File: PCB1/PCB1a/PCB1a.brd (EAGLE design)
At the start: 125.6 x 84.2 mm, 0 parts

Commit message: ,,
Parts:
- added HUB08RG, HUB12RG, HUB75RGB, HUB75RGB.: 61231620621, Wurth_Connectors_WR-BHD:61231620621
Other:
- board text added: "HUB08 RG"
- board text added: "HUB12 RG"
- board text added: "HUB75 RGB"

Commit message: .
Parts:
- added J1: 691318400002, Wurth_Connectors_WR-TBL Pluggable Connector:691318400002
- added J2: 691317410002, Wurth_Connectors_WR-TBL Pluggable Connector:691317410002
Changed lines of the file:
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@@
 <attribute name="WORKING-VOLTAGE" value="250V(AC)" x="-60.96" y="0" locked="yes" size="1.778" layer="27" display="off"/>
+</element>
+<element name="J1" library="Wurth_Connectors_WR-TBL Pluggable Connector" library_urn="urn:adsk.eagle:library:16280984" package="691318400002" package3d_urn="urn:adsk.eagle:package:16282433/2" value=" 691318400002 " x="30.48" y="48.26" smashed="yes">
+<attribute name="DATASHEET-URL" value="https://www.we-online.com/redexpert/spec/691318400002?ae" x="30.48" y="48.26" size="1.778" layer="27" display="off"/>
+<attribute name="IR-UL" value="20A" x="30.48" y="48.26" size="1.778" layer="27" display="off"/>
+<attribute name="MOUNT" value="THT" x="30.48" y="48.26" size="1.778" layer="27" display="off"/>
+<attribute name="NAME" x="30.48" y="53.76" size="1.27" layer="25" align="bottom-center"/>
+<attribute name="PART-NUMBER" value=" 691318400002 " x="30.48" y="48.26" size="1.778" layer="27" display="off"/>
+<attribute name="PINS" value=" 2 " x="30.48" y="48.26" size="1.778" layer="27" display="off"/>
+<attribute name="PITCH" value="7.62mm" x="30.48" y="48.26" size="1.778" layer="27" display="off"/>
+<attribute name="TYPE" value="Vertical" x="30.48" y="48.26" size="1.778" layer="27" display="off"/>
+<attribute name="VALUE" x="26.98" y="42.26" size="1.27" layer="27"/>
+<attribute name="WORKING-VOLTAGE-UL" value="300V (AC)" x="30.48" y="48.26" size="1.778" layer="27" display="off"/>
+</element>
+<element name="J2" library="Wurth_Connectors_WR-TBL Pluggable Connector" library_urn="urn:adsk.eagle:library:16280984" package="691317410002" package3d_urn="urn:adsk.eagle:package:16282458/2" value=" 691317410002 " x="-73.66" y="-60.96" smashed="yes">
+<attribute name="DATASHEET-URL" value="https://www.we-online.com/redexpert/spec/691317410002?ae" x="-73.66" y="-60.96" size="1.778" layer="27" display="off"/>
+<attribute name="IR-UL" value="20A" x="-73.66" y="-60.96" size="1.778" layer="27" display="off"/>
+<attribute name="MOUNT" value="THT" x="-73.66" y="-60.96" size="1.778" layer="27" display="off"/>
+<attribute name="NAME" x="-73.66" y="-57.96" size="1.27" layer="25" align="bottom-center"/>
+<attribute name="PART-NUMBER" value=" 691317410002 " x="-73.66" y="-60.96" size="1.778" layer="27" display="off"/>
+<attribute name="PINS" value=" 2 " x="-73.66" y="-60.96" size="1.778" layer="27" display="off"/>
+<attribute name="PITCH" value="7.62mm" x="-73.66" y="-60.96" size="1.778" layer="27" display="off"/>
+<attribute name="TYPE" value="Horizontal" x="-73.66" y="-60.96" size="1.778" layer="27" display="off"/>
+<attribute name="VALUE" x="-77.16" y="-72.96" size="1.27" layer="27"/>
+<attribute name="WORKING-VOLTAGE-UL" value="300V (AC)" x="-73.66" y="-60.96" size="1.778" layer="27" display="off"/>
 </element>
 </elements>

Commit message: power Conn. added.
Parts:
- removed J1: 691318400002, Wurth_Connectors_WR-TBL Pluggable Connector:691318400002
- removed J2: 691317410002, Wurth_Connectors_WR-TBL Pluggable Connector:691317410002
- added J3: 691325110005, Wurth_Connectors_WR-TBL Pluggable Connector:691325110005
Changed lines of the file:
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@@
 <setting verticaltext="up"/>
 </settings>
-<grid distance="100" unitdist="mil" unit="mil" style="lines" multiple="1" display="yes" altdistance="5" altunitdist="mil" altunit="mil"/>
+<grid distance="100" unitdist="mil" unit="mm" style="lines" multiple="1" display="yes" altdistance="5" altunitdist="mil" altunit="mil"/>
 <layers>
 <layer number="1" name="Top" color="4" fill="1" visible="yes" active="yes"/>
@@
 </layers>
 <board>
-<fusionsync huburn="a.YnVzaW5lc3M6bXNtdWM" projecturn="a.YnVzaW5lc3M6bXNtdWMjMjAyNDAxMTM3MTk1NzI4MDY" f3durn="urn:adsk.wipprod:dm.lineage:9HDWv57yTli2KPtb9bdN_w" pcbguid="128a00df-7ab4-4ae2-ad4e-bb8cbd2559b7" lastpulledtime="" lastsyncedchangeguid="" latestrevisionid="e052cb59-af4b-478b-bdef-e25eb81e0747" lastsyncedrevisionid="e052cb59-af4b-478b-bdef-e25eb81e0747" lastboardhashguid="e28fd9e1-8f83-2cc4-36d8-cf9d72c5d150" lastpushedtime="2024-01-13T22:40:11Z" linktopcb3d="true"/>
+<fusionsync huburn="a.YnVzaW5lc3M6bXNtdWM" projecturn="a.YnVzaW5lc3M6bXNtdWMjMjAyNDAxMTM3MTk1NzI4MDY" f3durn="urn:adsk.wipprod:dm.lineage:9HDWv57yTli2KPtb9bdN_w" pcbguid="" lastpulledtime="" lastsyncedchangeguid="" latestrevisionid="5f602aae-c13a-43fd-976a-559e74166529" lastsyncedrevisionid="5f602aae-c13a-43fd-976a-559e74166529" lastboardhashguid="a5968208-0cce-2099-51f9-27230b5d76be" lastpushedtime="2024-01-14T11:15:05Z" linktopcb3d="true"/>
 <plain>
 <wire x1="-75" y1="40.6" x2="-75" y2="-40.6" width="0" layer="20" locked="yes"/>
@@
 <attribute name="WORKING-VOLTAGE" value="250V(AC)" x="-60.96" y="0" locked="yes" size="1.778" layer="27" display="off"/>
 </element>
-<element name="J1" library="Wurth_Connectors_WR-TBL Pluggable Connector" library_urn="urn:adsk.eagle:library:16280984" package="691318400002" package3d_urn="urn:adsk.eagle:package:16282433/2" value=" 691318400002 " x="30.48" y="48.26" smashed="yes">
-<attribute name="DATASHEET-URL" value="https://www.we-online.com/redexpert/spec/691318400002?ae" x="30.48" y="48.26" size="1.778" layer="27" display="off"/>
-<attribute name="IR-UL" value="20A" x="30.48" y="48.26" size="1.778" layer="27" display="off"/>
-<attribute name="MOUNT" value="THT" x="30.48" y="48.26" size="1.778" layer="27" display="off"/>
-<attribute name="NAME" x="30.48" y="53.76" size="1.27" layer="25" align="bottom-center"/>
-<attribute name="PART-NUMBER" value=" 691318400002 " x="30.48" y="48.26" size="1.778" layer="27" display="off"/>
-<attribute name="PINS" value=" 2 " x="30.48" y="48.26" size="1.778" layer="27" display="off"/>
-<attribute name="PITCH" value="7.62mm" x="30.48" y="48.26" size="1.778" layer="27" display="off"/>
-<attribute name="TYPE" value="Vertical" x="30.48" y="48.26" size="1.778" layer="27" display="off"/>
-<attribute name="VALUE" x="26.98" y="42.26" size="1.27" layer="27"/>
-<attribute name="WORKING-VOLTAGE-UL" value="300V (AC)" x="30.48" y="48.26" size="1.778" layer="27" display="off"/>
-</element>
-<element name="J2" library="Wurth_Connectors_WR-TBL Pluggable Connector" library_urn="urn:adsk.eagle:library:16280984" package="691317410002" package3d_urn="urn:adsk.eagle:package:16282458/2" value=" 691317410002 " x="-73.66" y="-60.96" smashed="yes">
-<attribute name="DATASHEET-URL" value="https://www.we-online.com/redexpert/spec/691317410002?ae" x="-73.66" y="-60.96" size="1.778" layer="27" display="off"/>
-<attribute name="IR-UL" value="20A" x="-73.66" y="-60.96" size="1.778" layer="27" display="off"/>
-<attribute name="MOUNT" value="THT" x="-73.66" y="-60.96" size="1.778" layer="27" display="off"/>
-<attribute name="NAME" x="-73.66" y="-57.96" size="1.27" layer="25" align="bottom-center"/>
-<attribute name="PART-NUMBER" value=" 691317410002 " x="-73.66" y="-60.96" size="1.778" layer="27" display="off"/>
-<attribute name="PINS" value=" 2 " x="-73.66" y="-60.96" size="1.778" layer="27" display="off"/>
-<attribute name="PITCH" value="7.62mm" x="-73.66" y="-60.96" size="1.778" layer="27" display="off"/>
-<attribute name="TYPE" value="Horizontal" x="-73.66" y="-60.96" size="1.778" layer="27" display="off"/>
-<attribute name="VALUE" x="-77.16" y="-72.96" size="1.27" layer="27"/>
-<attribute name="WORKING-VOLTAGE-UL" value="300V (AC)" x="-73.66" y="-60.96" size="1.778" layer="27" display="off"/>
+<element name="J3" library="Wurth_Connectors_WR-TBL Pluggable Connector" library_urn="urn:adsk.eagle:library:16280984" package="691325110005" package3d_urn="urn:adsk.eagle:package:16281816/2" value=" 691325110005 " x="27.94" y="-34.1" smashed="yes">
+<attribute name="DATASHEET-URL" value="https://www.we-online.com/redexpert/spec/691325110005?ae" x="27.94" y="-34.1" size="1.778" layer="27" display="off"/>
+<attribute name="IR-UL" value="10A" x="27.94" y="-34.1" size="1.778" layer="27" display="off"/>
+<attribute name="IR-VDE" value="10.5A" x="27.94" y="-34.1" size="1.778" layer="27" display="off"/>
+<attribute name="MOUNT" value="THT" x="27.94" y="-34.1" size="1.778" layer="27" display="off"/>
+<attribute name="NAME" x="27.94" y="-32.1" size="1.27" layer="25" align="bottom-center"/>
+<attribute name="PART-NUMBER" value=" 691325110005 " x="27.94" y="-34.1" size="1.778" layer="27" display="off"/>
+<attribute name="PINS" value=" 5 " x="27.94" y="-34.1" size="1.778" layer="27" display="off"/>
+<attribute name="PITCH" value="3.5mm" x="27.94" y="-34.1" size="1.778" layer="27" display="off"/>
+<attribute name="TYPE" value="Horizontal" x="27.94" y="-34.1" size="1.778" layer="27" display="off"/>
+<attribute name="VALUE" x="24.44" y="-44.1" size="1.27" layer="27"/>
+<attribute name="WORKING-VOLTAGE-UL" value="300V (AC)" x="27.94" y="-34.1" size="1.778" layer="27" display="off"/>
+<attribute name="WORKING-VOLTAGE-VDE" value="300V (AC)" x="27.94" y="-34.1" size="1.778" layer="27" display="off"/>
 </element>
 </elements>

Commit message: -
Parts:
- removed J3: 691325110005, Wurth_Connectors_WR-TBL Pluggable Connector:691325110005
- added J1: 691357310006B, Wurth_Connectors_WR-TBL Pluggable Connector:691357310006B
- added U8, U9: 74AHCT245, microbuilder:TSSOP20
- moved HUB75RGB 22.9 mm to (-61.0, -8.89)
- moved HUB12RG 8.89 mm to (-61.0, 8.89)
- moved HUB08RG 1.27 mm to (-61.0, 26.7)
- moved HUB75RGB. 1.27 mm to (-61.0, -26.7)
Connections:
- new net +5V: U8.1, U8.20, U9.1, U9.20
- new net ADDRA_3V: U8.5
- new net ADDRB_3V: U9.9
- new net ADDRC_3V: U8.6
- new net ADDRD_3V: U8.4
- new net ADDRE_3V: U8.8
- new net B1_3V: U9.4
- new net B2_3V: U9.7
- new net CLK_3V: U9.8
- new net G1_3V: U9.3
- new net G2_3V: U9.5
- new net GND: HUB08RG.1, HUB08RG.13, HUB08RG.15, HUB08RG.3, HUB08RG.5, HUB12RG.11, HUB12RG.13, HUB12RG.15, HUB12RG.3, HUB12RG.5, HUB12RG.7, HUB12RG.9, HUB75RGB..16, HUB75RGB..4, HUB75RGB..8, HUB75RGB.16, HUB75RGB.4, HUB75RGB.8, U8.10, U8.19, U8.2, U8.3, U9.10, U9.19
- new net LAT_3V: U8.7
- new net M1_A: HUB08RG.2, HUB12RG.2, HUB75RGB..9, HUB75RGB.9, U8.15
- new net M1_B: HUB08RG.4, HUB12RG.4, HUB75RGB..10, HUB75RGB.10, U9.11
- new net M1_B1: HUB75RGB..3, HUB75RGB.3, U9.16
- new net M1_B2: HUB75RGB..7, HUB75RGB.7, U9.13
- new net M1_C: HUB08RG.6, HUB12RG.6, HUB75RGB..11, HUB75RGB.11, U8.14
- new net M1_CLK: HUB08RG.16, HUB12RG.8, HUB75RGB..13, HUB75RGB.13, U9.12
- new net M1_D: HUB08RG.8, HUB12RG.16, HUB75RGB..12, HUB75RGB.12, U8.16
- new net M1_E: U8.12
- new net M1_G1: HUB08RG.10, HUB12RG.14, HUB75RGB..2, HUB75RGB.2, U9.17
- new net M1_G2: HUB08RG.12, HUB75RGB..6, HUB75RGB.6, U9.15
- new net M1_LAT: HUB08RG.14, HUB12RG.10, HUB75RGB..14, HUB75RGB.14, U8.13
- new net M1_OE: HUB08RG.7, HUB12RG.1, HUB75RGB..15, HUB75RGB.15, U8.11
- new net M1_R1: HUB08RG.9, HUB12RG.12, HUB75RGB..1, HUB75RGB.1, U9.18
- new net M1_R2: HUB08RG.11, HUB75RGB..5, HUB75RGB.5, U9.14
- new net OE_3V: U8.9
- new net R1_3V: U9.2
- new net R2_3V: U9.6
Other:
- board text added: "A"
- board text added: "B"
- board text added: "B0"
- board text added: "B1"
- board text added: "C"
- board text added: "CK"
- board text added: "D"
- board text added: "D:/SmartProjects/Snc/a4_bn_logo2.bmp"
- board text added: "G0"
- board text added: "G1"
- board text added: "LT"
- board text added: "OE"
- board text added: "R0"
- board text added: "R1"

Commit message: ..
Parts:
- added J2: 618009231421, Wurth_Connectors_WR-DSUB:618009231421
- added T1: 7498011211, Wurth_Signal & Communications_WE-RJ45_LAN:7498011211
- moved J1 27.9 mm to (2.54, -27.8)
- moved U8 7.58 mm to (-33.7, -14.6)
- moved U9 7.37 mm to (-33.7, -21.6)
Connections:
- new net CAN_H: J1.6
- new net CAN_L: J1.5
- new net RX: J2.2
- new net TX: J2.3
- net +5V: now also J1.3
- net GND: now also J1.1, J1.4, J2.5, J2.S1, J2.S2
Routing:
- net M1_R1: track 0.00 -> 124.3 mm, vias 0 -> 6
- net M1_G1: track 0.00 -> 122.4 mm, vias 0 -> 6
- net M1_A: track 0.00 -> 96.4 mm, vias 0 -> 4
- net M1_B: track 0.00 -> 94.9 mm, vias 0 -> 4
- net M1_G2: track 0.00 -> 93.5 mm, vias 0 -> 4
- net M1_D: track 0.00 -> 93.4 mm, vias 0 -> 4
- net M1_OE: track 0.00 -> 93.1 mm, vias 0 -> 4
- net M1_CLK: track 0.00 -> 91.5 mm, vias 0 -> 4
- net M1_C: track 0.00 -> 90.6 mm, vias 0 -> 2
- net M1_R2: track 0.00 -> 90.1 mm, vias 0 -> 4
- net M1_LAT: track 0.00 -> 86.4 mm, vias 0 -> 6
- net M1_B1: track 0.00 -> 55.2 mm, vias 0 -> 2
- net GND: track 0.00 -> 52.1 mm, vias 0 -> 15
- net M1_B2: track 0.00 -> 45.9 mm, vias 0 -> 2
- net +5V: track 0.00 -> 6.37 mm, vias 0 -> 4
- added copper zone on layer 15, net +5V
- added copper zone on layer 2, net GND

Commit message: ethernet remove for now.
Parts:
- removed T1: 7498011211, Wurth_Signal & Communications_WE-RJ45_LAN:7498011211
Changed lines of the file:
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@@
 <drawing>
 <settings>
-<setting alwaysvectorfont="yes"/>
+<setting alwaysvectorfont="no"/>
 <setting verticaltext="up"/>
 </settings>
@@
 <attribute name="WORKING-VOLTAGE" value="125 V(AC)" x="45.955" y="16.51" size="1.778" layer="27" rot="R90" display="off"/>
 </element>
-<element name="T1" library="Wurth_Signal &amp; Communications_WE-RJ45_LAN" library_urn="urn:adsk.eagle:library:14284239" package="7498011211" package3d_urn="urn:adsk.eagle:package:12863525/4" value=" 7498011211 " x="40.64" y="-22.86" smashed="yes" rot="R90">
-<attribute name="DATA-RATE" value="10/100 Base-T" x="40.64" y="-22.86" size="1.778" layer="27" rot="R90" display="off"/>
-<attribute name="DATASHEET-URL" value="https://www.we-online.com/redexpert/spec/7498011211?ae" x="40.64" y="-22.86" size="1.778" layer="27" rot="R90" display="off"/>
-<attribute name="LED" value="green-yellow" x="40.64" y="-22.86" size="1.778" layer="27" rot="R90" display="off"/>
-<attribute name="MOUNT" value="SMT" x="40.64" y="-22.86" size="1.778" layer="27" rot="R90" display="off"/>
-<attribute name="NAME" x="27.14" y="-22.86" size="1.27" layer="25" rot="R90" align="bottom-center"/>
-<attribute name="PART-NUMBER" value=" 7498011211 " x="40.64" y="-22.86" size="1.778" layer="27" rot="R90" display="off"/>
-<attribute name="POE" value="non-PoE" x="40.64" y="-22.86" size="1.778" layer="27" rot="R90" display="off"/>
-<attribute name="PORTS" value=" 1 " x="40.64" y="-22.86" size="1.778" layer="27" rot="R90" display="off"/>
-<attribute name="USB" value="No" x="40.64" y="-22.86" size="1.778" layer="27" rot="R90" display="off"/>
-<attribute name="VALUE" x="53.64" y="-22.86" size="1.27" layer="27" rot="R90" align="bottom-center"/>
-</element>
 </elements>

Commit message: so far ...
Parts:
- added J3: ESP32_DEVC_MIN_LEFT, eclibrary:ESP32_DEVC_DUAL_HEADER_BOT_MOUNT_LEFT
- added J4: ESP32_DEVC_MIN_RIGHT, eclibrary:ESP32_DEVC_DUAL_HEADER_BOT_MOUNT_RIGHT
- moved J1 27.9 mm to (30.5, -27.8)
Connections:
- new net 3V3: J4.3V3A, J4.3V3B
- new net N$10: J4.VPA, J4.VPB
- new net N$11: J4.34A, J4.34B
- new net N$13: J4.ENA, J4.ENB
- new net N$14: J3.TXA, J3.TXB
- new net N$15: J3.RXA, J3.RXB
- new net N$16: J3.17A_A, J3.17B_B
- new net N$17: J3.16A_A, J3.16_B
- new net N$2: J4.CMD_A, J4.CMD_B
- new net N$3: J4.D3_A, J4.D3_B
- new net N$5: J4.D2A, J4.D2B
- new net N$6: J3.CLKA, J3.CLKB
- new net N$7: J3.D0A, J3.D0B
- new net N$8: J3.D1A, J3.D1B
- new net N$9: J4.VNA, J4.VNB
- new net VIN: J4.5V_A, J4.5V_B
- net ADDRA_3V: now also J3.19A_A, J3.19B_B
- net ADDRB_3V: now also J3.22A, J3.22B
- net ADDRC_3V: now also J3.21A, J3.21B
- net ADDRD_3V: now also J3.4A, J3.4B
- net ADDRE_3V: now also J4.26A, J4.26B
- net B1_3V: now also J4.33A, J4.33B
- net B2_3V: now also J3.18A_A, J3.18B_B
- net CLK_3V: now also J3.2A, J3.2B
- net G1_3V: now also J4.14A_A, J4.14B_B
- net G2_3V: now also J4.27A, J4.27B
- net GND: now also J3.GND1A, J3.GND1B, J3.GNDA, J3.GNDB, J4.GNDA, J4.GNDB; no longer HUB75RGB..8, HUB75RGB.8
- net LAT_3V: now also J3.15A_A, J3.15B_B
- net M1_E: now also HUB75RGB..8, HUB75RGB.8
- net OE_3V: now also J4.13A_A, J4.13B_B
- net R1_3V: now also J4.12A, J4.12B
- net R2_3V: now also J4.25A, J4.25B
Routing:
- net M1_E: track 0.00 -> 18.6 mm
- net GND: track 52.1 -> 48.7 mm, vias 15 -> 14

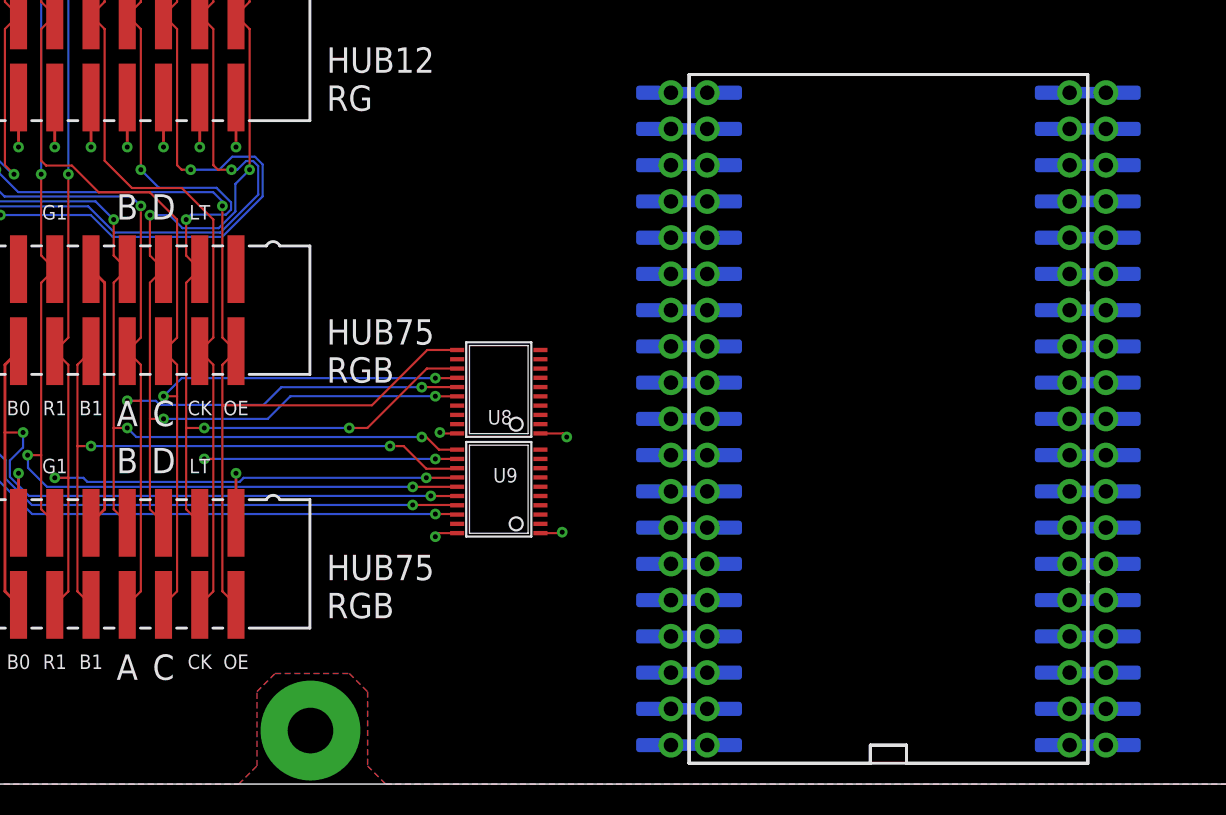
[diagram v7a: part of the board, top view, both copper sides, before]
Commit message: ESP32 added.
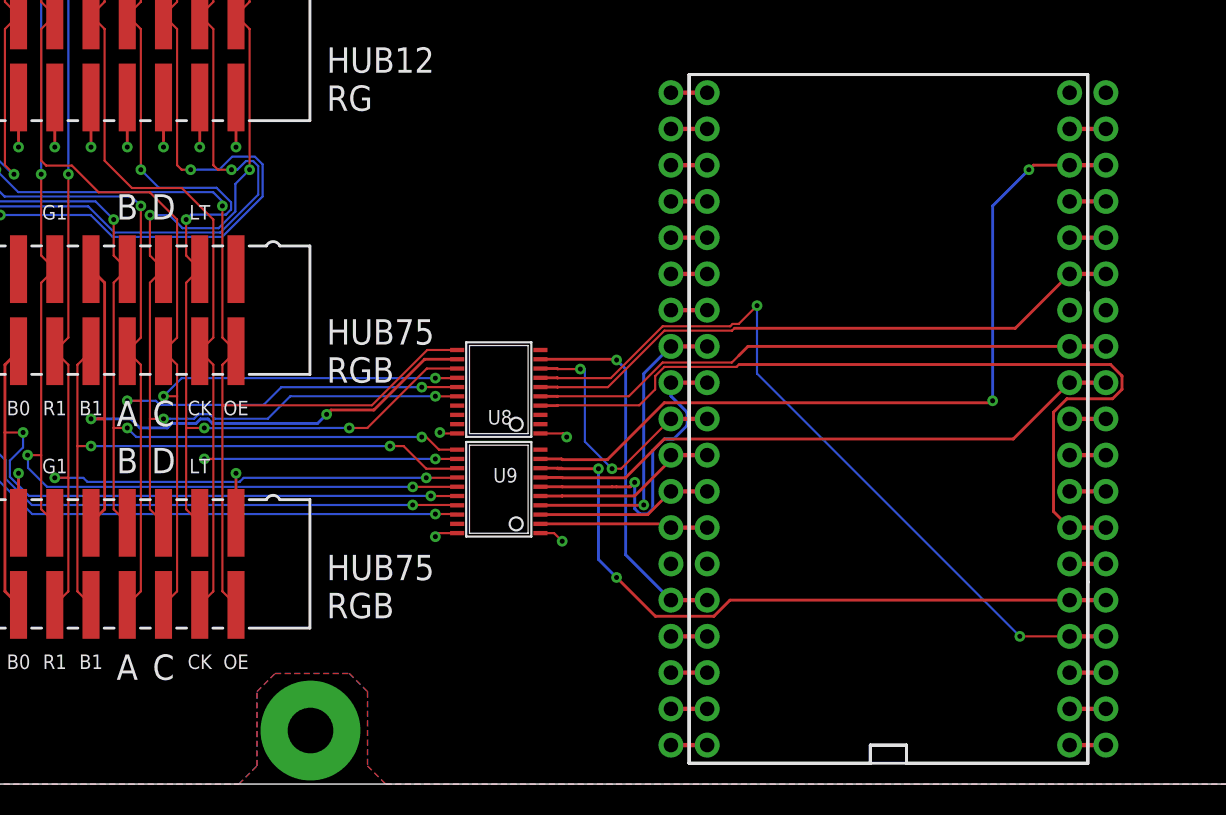
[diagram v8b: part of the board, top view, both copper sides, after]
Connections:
- removed net VIN: J4.5V_A, J4.5V_B
- new net N$1: J3.0A, J3.0B
- new net N$12: J3.23A, J3.23B
- new net N$18: J4.35A, J4.35B
- new net N$19: J4.32A, J4.32B
- new net N$4: J3.5A, J3.5B
- net +5V: now also J4.5V_A, J4.5V_B
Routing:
- net ADDRD_3V: track 0.00 -> 60.3 mm
- net ADDRB_3V: track 0.00 -> 56.8 mm, vias 0 -> 2
- net LAT_3V: track 0.00 -> 54.1 mm, vias 0 -> 2
- net CLK_3V: track 0.00 -> 48.4 mm, vias 0 -> 2
- net ADDRC_3V: track 0.00 -> 42.9 mm
- net B2_3V: track 0.00 -> 42.4 mm
- net ADDRA_3V: track 0.00 -> 41.1 mm
- net M1_E: track 18.6 -> 47.7 mm, vias 0 -> 2
- net OE_3V: track 0.00 -> 26.3 mm, vias 0 -> 1
- net R2_3V: track 0.00 -> 23.4 mm, vias 0 -> 1
- net B1_3V: track 0.00 -> 21.7 mm, vias 0 -> 1
- net ADDRE_3V: track 0.00 -> 19.0 mm, vias 0 -> 2
- net G2_3V: track 0.00 -> 13.1 mm
- net G1_3V: track 0.00 -> 12.4 mm
- net R1_3V: track 0.00 -> 11.8 mm
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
